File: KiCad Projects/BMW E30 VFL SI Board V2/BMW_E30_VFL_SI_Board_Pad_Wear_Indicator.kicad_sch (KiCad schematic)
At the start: 11 parts, among them Q8 BC327-16

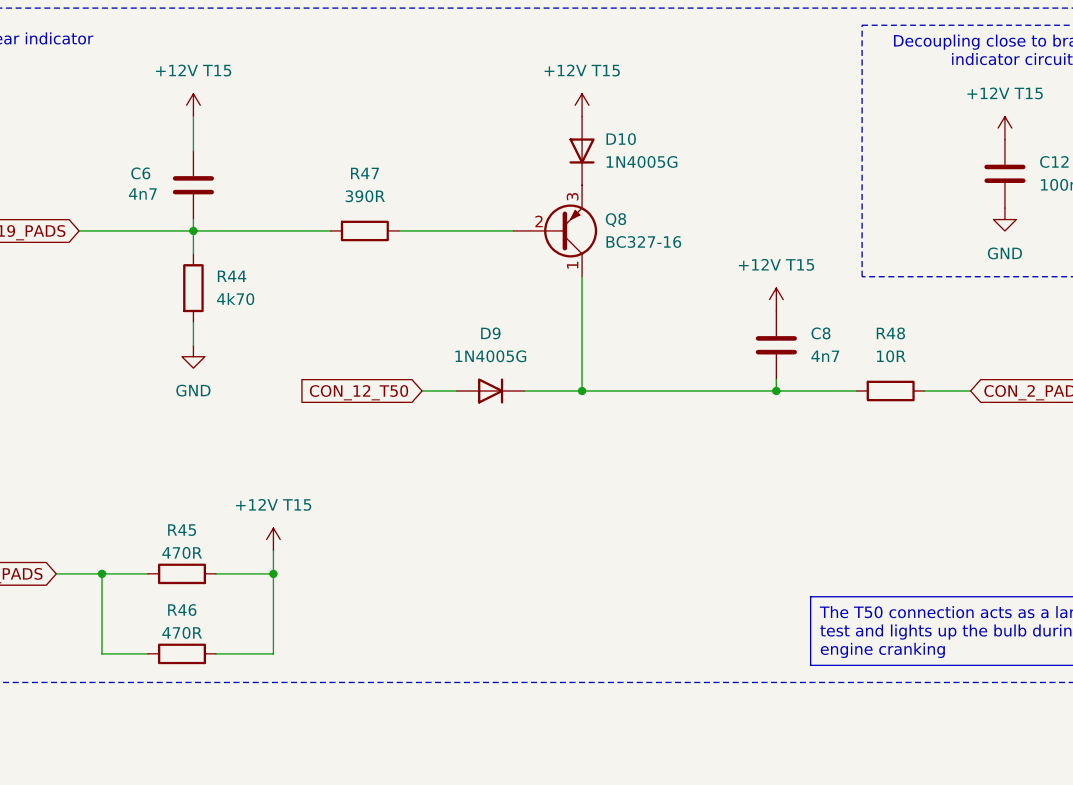
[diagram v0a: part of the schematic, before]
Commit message: Bugfixing of component designators
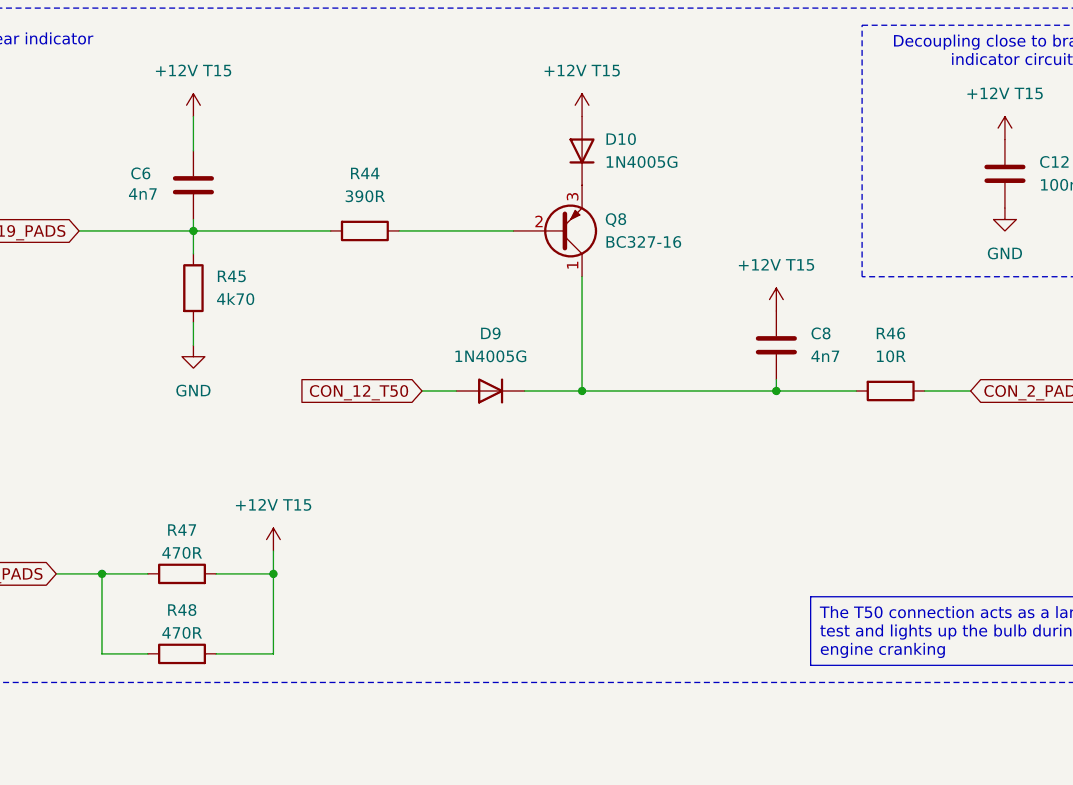
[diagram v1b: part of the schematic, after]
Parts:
- renumbered R47 to R44, R44 to R45, R48 to R46, R45 to R47, R46 to R48
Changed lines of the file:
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@@
 		(dnp no)
 		(fields_autoplaced yes)
-		(property "Reference" "R48"
+		(property "Reference" "R46"
 			(at 185.42 87.63 90)
 			(effects
@@
 			(project "BMW E30 VFL SI Board V2"
 				(path "/b9f8b657-f23f-4f46-b33b-c9c07ea00dca/06cb897c-0efb-438a-95e3-30e073586624"
-					(reference "R48")
+					(reference "R46")
 					(unit 1)
 				)
@@
 		(on_board yes)
 		(dnp no)
-		(property "Reference" "R46"
+		(property "Reference" "R48"
 			(at 106.68 118.364 90)
 			(effects
@@
 			(project "BMW E30 VFL SI Board V2"
 				(path "/b9f8b657-f23f-4f46-b33b-c9c07ea00dca/06cb897c-0efb-438a-95e3-30e073586624"
-					(reference "R46")
+					(reference "R48")
 					(unit 1)
 				)
@@
 		(dnp no)
 		(fields_autoplaced yes)
-		(property "Reference" "R47"
+		(property "Reference" "R44"
 			(at 127 69.85 90)
 			(effects
@@
 			(project "BMW E30 VFL SI Board V2"
 				(path "/b9f8b657-f23f-4f46-b33b-c9c07ea00dca/06cb897c-0efb-438a-95e3-30e073586624"
-					(reference "R47")
+					(reference "R44")
 					(unit 1)
 				)
@@
 		(dnp no)
 		(fields_autoplaced yes)
-		(property "Reference" "R44"
+		(property "Reference" "R45"
 			(at 110.49 81.2799 0)
 			(effects
@@
 			(project "BMW E30 VFL SI Board V2"
 				(path "/b9f8b657-f23f-4f46-b33b-c9c07ea00dca/06cb897c-0efb-438a-95e3-30e073586624"
-					(reference "R44")
+					(reference "R45")
 					(unit 1)
 				)
@@
 		(on_board yes)
 		(dnp no)
-		(property "Reference" "R45"
+		(property "Reference" "R47"
 			(at 106.68 109.474 90)
 			(effects
@@
 			(project "BMW E30 VFL SI Board V2"
 				(path "/b9f8b657-f23f-4f46-b33b-c9c07ea00dca/06cb897c-0efb-438a-95e3-30e073586624"
-					(reference "R45")
-					(unit 1)
-				)
+					(reference "R47")
+					(unit 1)
+				)
